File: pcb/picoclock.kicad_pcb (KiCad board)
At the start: 2 copper layers, 175.8 x 64 mm, 87 parts, among them J1 UART, J10 USB, J11 Alt Power, J12 PWM, J13 AUDIO, J15 Conn_01x24, J2 AUDIO, J3 xx, J4 xx, J5 Micro_SD_Card_Det1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

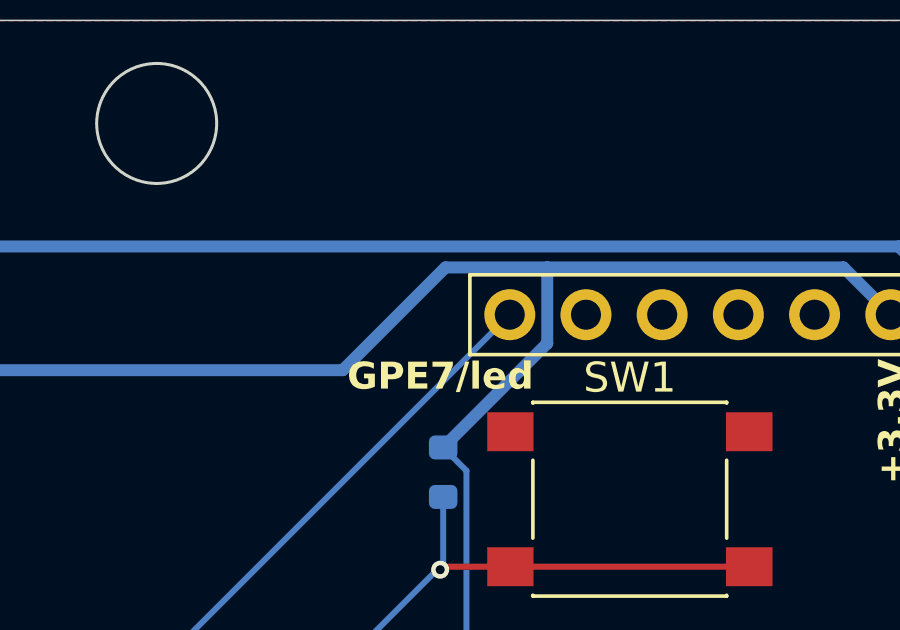
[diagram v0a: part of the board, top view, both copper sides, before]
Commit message: [pcb] add pullup resistor for MCP23009
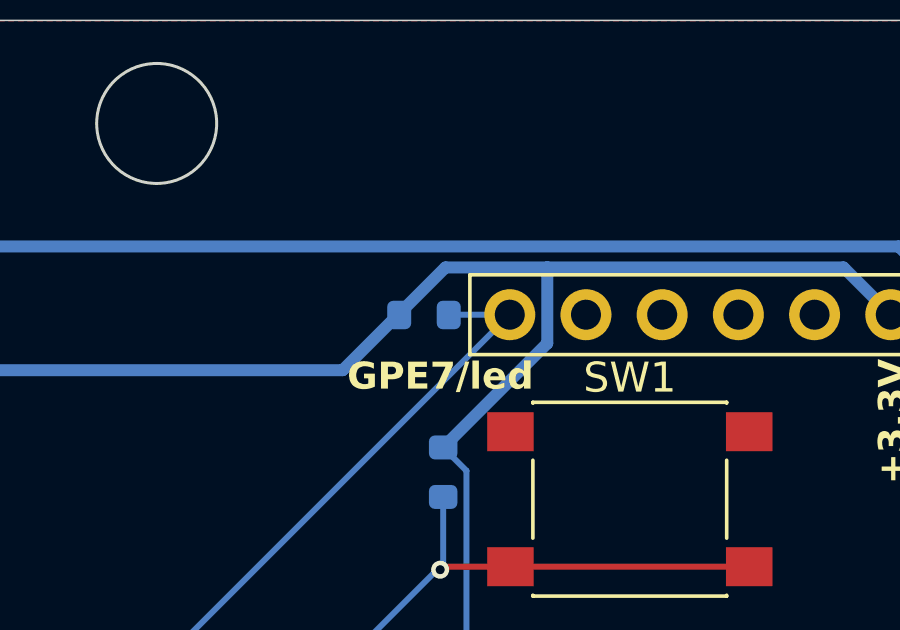
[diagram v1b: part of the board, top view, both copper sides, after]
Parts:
- added R17: 10K, Resistor_SMD:R_0603_1608Metric, B.Cu at (188.5, 76.7)
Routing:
- net GPE7/led: track 54.3 -> 56.4 mm
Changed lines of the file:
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@@
 		)
 	)
+	(footprint "Resistor_SMD:R_0603_1608Metric"
+		(layer "B.Cu")
+		(at 188.46 76.71)
+		(descr "Resistor SMD 0603 (1608 Metric), square (rectangular) end terminal, IPC_7351 nominal, (Body size source: IPC-SM-782 page 72, https://www.pcb-3d.com/wordpress/wp-content/uploads/ipc-sm-782a_amendment_1_and_2.pdf), generated with kicad-footprint-generator")
+		(tags "resistor")
+		(property "Reference" "R17"
+			(at -2.83 -0.04 360)
+			(layer "B.SilkS")
+			(effects
+				(font
+					(size 1 1)
+					(thickness 0.15)
+				)
+				(justify mirror)
+			)
+		)
+		(property "Value" "10K"
+			(at -5.86 -0.01 0)
+			(layer "B.SilkS")
+			(effects
+				(font
+					(size 1 1)
+					(thickness 0.15)
+				)
+				(justify mirror)
+			)
+		)
+		(property "Footprint" "Resistor_SMD:R_0603_1608Metric"
+			(at 0 0 180)
+			(unlocked yes)
+			(layer "B.Fab")
+			(hide yes)
+			(effects
+				(font
+					(size 1.27 1.27)
+					(thickness 0.15)
+				)
+				(justify mirror)
+			)
+		)
+		(property "Datasheet" ""
+			(at 0 0 180)
+			(unlocked yes)
+			(layer "B.Fab")
+			(hide yes)
+			(effects
+				(font
+					(size 1.27 1.27)
+					(thickness 0.15)
+				)
+				(justify mirror)
+			)
+		)
+		(property "Description" ""
+			(at 0 0 180)
+			(unlocked yes)
+			(layer "B.Fab")
+			(hide yes)
+			(effects
+				(font
+					(size 1.27 1.27)
+					(thickness 0.15)
+				)
+				(justify mirror)
+			)
+		)
+		(property "LCSC" "C25744"
+			(at 0 0 180)
+			(unlocked yes)
+			(layer "B.Fab")
+			(hide yes)
+			(effects
+				(font
+					(size 1 1)
+					(thickness 0.15)
+				)
+				(justify mirror)
+			)
+		)
+		(property ki_fp_filters "R_*")
+		(sheetname "Root")
+		(sheetfile "picoclock.kicad_sch")
+		(attr smd)
+		(fp_line
+			(start 0.237258 -0.5225)
+			(end -0.237258 -0.5225)
+			(stroke
+				(width 0.12)
+				(type solid)
+			)
+			(layer "B.SilkS")
+		)
+		(fp_line
+			(start 0.237258 0.5225)
+			(end -0.237258 0.5225)
+			(stroke
+				(width 0.12)
+				(type solid)
+			)
+			(layer "B.SilkS")
+		)
+		(fp_line
+			(start -1.48 -0.73)
+			(end 1.48 -0.73)
+			(stroke
+				(width 0.05)
+				(type solid)
+			)
+			(layer "B.CrtYd")
+		)
+		(fp_line
+			(start -1.48 0.73)
+			(end -1.48 -0.73)
+			(stroke
+				(width 0.05)
+				(type solid)
+			)
+			(layer "B.CrtYd")
+		)
+		(fp_line
+			(start 1.48 -0.73)
+			(end 1.48 0.73)
+			(stroke
+				(width 0.05)
+				(type solid)
+			)
+			(layer "B.CrtYd")
+		)
+		(fp_line
+			(start 1.48 0.73)
+			(end -1.48 0.73)
+			(stroke
+				(width 0.05)
+				(type solid)
+			)
+			(layer "B.CrtYd")
+		)
+		(fp_line
+			(start -0.8 -0.4125)
+			(end 0.8 -0.4125)
+			(stroke
+				(width 0.1)
+				(type solid)
+			)
+			(layer "B.Fab")
+		)
+		(fp_line
+			(start -0.8 0.4125)
+			(end -0.8 -0.4125)
+			(stroke
+				(width 0.1)
+				(type solid)
+			)
+			(layer "B.Fab")
+		)
+		(fp_line
+			(start 0.8 -0.4125)
+			(end 0.8 0.4125)
+			(stroke
+				(width 0.1)
+				(type solid)
+			)
+			(layer "B.Fab")
+		)
+		(fp_line
+			(start 0.8 0.4125)
+			(end -0.8 0.4125)
+			(stroke
+				(width 0.1)
+				(type solid)
+			)
+			(layer "B.Fab")
+		)
+		(fp_text user "${REFERENCE}"
+			(at 0 0 360)
+			(layer "B.Fab")
+			(effects
+				(font
+					(size 0.4 0.4)
+					(thickness 0.06)
+				)
+				(justify mirror)
+			)
+		)
+		(pad "1" smd roundrect
+			(at -0.825 0)
+			(size 0.8 0.95)
+			(layers "B.Cu" "B.Paste" "B.Mask")
+			(roundrect_rratio 0.25)
+			(net 2 "+3.3V")
+			(pintype "passive")
+		)
+		(pad "2" smd roundrect
+			(at 0.825 0)
+			(size 0.8 0.95)
+			(layers "B.Cu" "B.Paste" "B.Mask")
+			(roundrect_rratio 0.25)
+			(net 55 "GPE7{slash}led")
+			(pintype "passive")
+		)
+		(model "${KICAD8_3DMODEL_DIR}/Resistor_SMD.3dshapes/R_0603_1608Metric.wrl"
+			(offset
+				(xyz 0 0 0)
+			)
+			(scale
+				(xyz 1 1 1)
+			)
+			(rotate
+				(xyz 0 0 0)
+			)
+		)
+	)
 	(footprint "Capacitor_SMD:C_0603_1608Metric"
 		(layer "B.Cu")
@@
 		)
 	)
-	(gr_text "+3.3V"
-		(at 189.3955 72.375 90)
-		(layer "B.SilkS")
-		(effects
-			(font
-				(size 0.9 0.9)
-				(thickness 0.15)
-				(bold yes)
-			)
-			(justify left bottom mirror)
-		)
-	)
 	(gr_text "CLK"
 		(at 170.425 83.025 0)
@@
 		(width 0.2)
 		(layer "B.Cu")
+		(net 55)
+	)
+	(segment
+		(start 189.295 76.7)
+		(end 189.285 76.71)
+		(width 0.2)
+		(layer "B.Cu")
+		(net 55)
+	)
+	(segment
+		(start 191.32 76.7)
+		(end 189.295 76.7)
+		(width 0.2)
+		(layer "B.Cu")

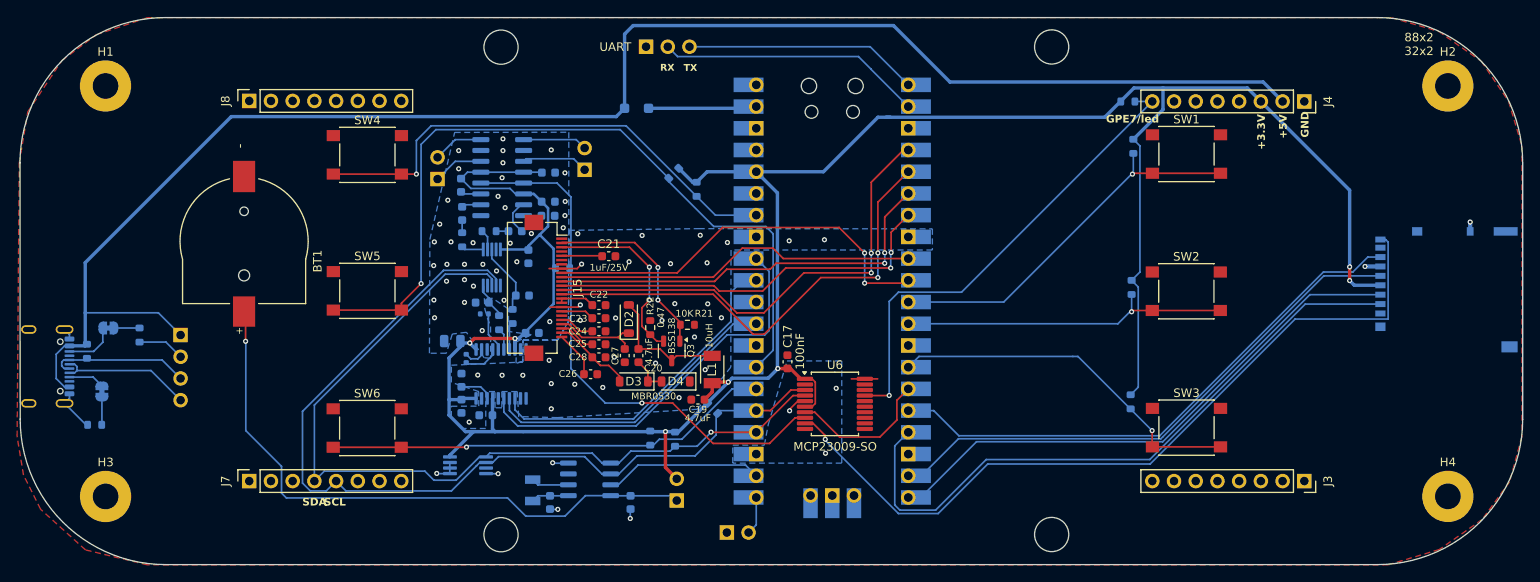
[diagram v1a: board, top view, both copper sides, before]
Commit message: [pcb] move battery holder, other small tweaks
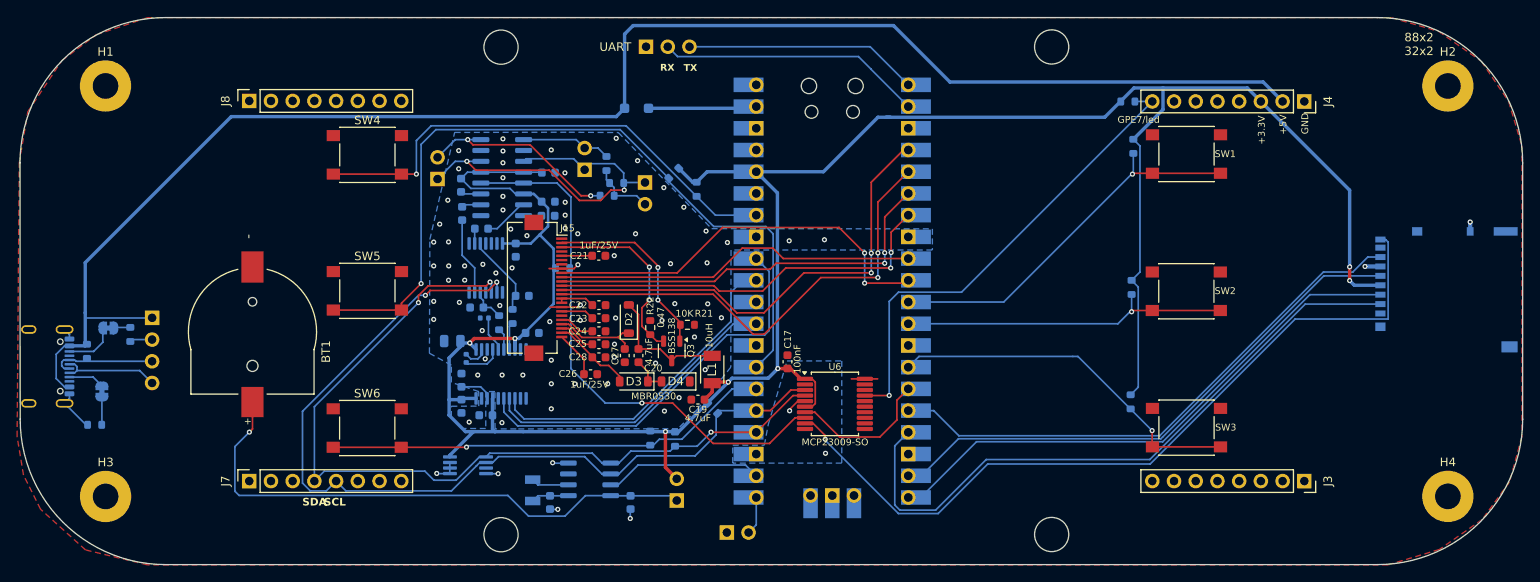
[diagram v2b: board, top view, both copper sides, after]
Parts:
- added J9: AUDIO, Connector_PinHeader_2.54mm:PinHeader_1x02_P2.54mm_Vertical, B.Cu at (132.0, 86.2)
- added R18: 10K, Resistor_SMD:R_0603_1608Metric, B.Cu at (128.7, 86.2)
- R14, R15: value 470 -> 10K
- U7: value MCP4652T -> MCP4652-104E; footprint Package_SO:MSOP-10_3x3mm_P0.5mm -> Package_SO:TSSOP-14_4.4x5mm_P0.65mm
- moved R14 17.7 mm to (127.6, 87.7), turned to 180 degrees
- moved R15 15.8 mm to (127.5, 84.0), turned to 90 degrees
- moved BT1 10.6 mm to (86.1, 103.6)
- moved C18 3.95 mm to (112.9, 91.6)
- moved J10 3.89 mm to (74.3, 102.0)
- moved C15 1.66 mm to (116.9, 94.1)
- moved C21 1.17 mm to (126.6, 94.8)
- moved R5 1.08 mm to (71.8, 104.0)
- moved C10 0.86 mm to (112.3, 100.8)
- moved U7 0.71 mm to (113.4, 96.2)
- moved C8 0.48 mm to (113.2, 102.0)
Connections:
- C18 pad 1: Net-(C18-Pad1) -> Net-(U7-P0W)
- C29 pad 1: Net-(C29-Pad1) -> Net-(U7-P1W)
- J2 pad 1: AUDIO_OUT_R- -> AUDIO_OUT_L-
- R14 pad 1: Net-(U7-P1W) -> MONO_OUT_R+
- R14 pad 2: Net-(C29-Pad1) -> AUDIO_OUT_R+
- R15 pad 1: Net-(C18-Pad1) -> MONO_OUT_R+
- R15 pad 2: Net-(U7-P0W) -> AUDIO_OUT_L+
- U5 pad 14: AUDIO_OUT_R- -> AUDIO_OUT_L-
- U7 pad 10: +3.3V -> LINE_OUT_RIGHT
- U7 pad 7: Net-(U7-P0W) -> GND
- U7 pad 8: LINE_OUT_RIGHT -> GND
- U7 pad 9: GND -> Net-(U7-P0W)
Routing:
- net AUDIO_OUT_L-: track 7.79 -> 44.4 mm, vias 0 -> 2
- net AUDIO_OUT_R+: track 5.92 -> 24.1 mm, vias 0 -> 2
- net MONO_OUT_R+: track 0.00 -> 7.33 mm
- net Net-(U7-P1W): track 2.60 -> 9.07 mm
- net 3V BATT: track 71.7 -> 65.5 mm
- net AUDIO_OUT_R-: track 5.92 -> 0.00 mm
- net +5V: track 190.9 -> 186.5 mm
- net USB D-: track 16.0 -> 11.8 mm
- net USB D+: track 16.4 -> 12.2 mm
- net GND: track 38.6 -> 35.4 mm, vias 76 -> 82
- net AUDIO_OUT_L+: track 7.54 -> 10.5 mm
- net Net-(C29-Pad1): track 1.47 -> 0.00 mm
- net Net-(C18-Pad1): track 1.45 -> 0.00 mm
- net LINE_OUT_RIGHT: track 8.33 -> 9.57 mm
- net Net-(J15-Pin_5): track 4.75 -> 3.56 mm
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
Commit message: [pcb] mono audio, combined sdcard footprint
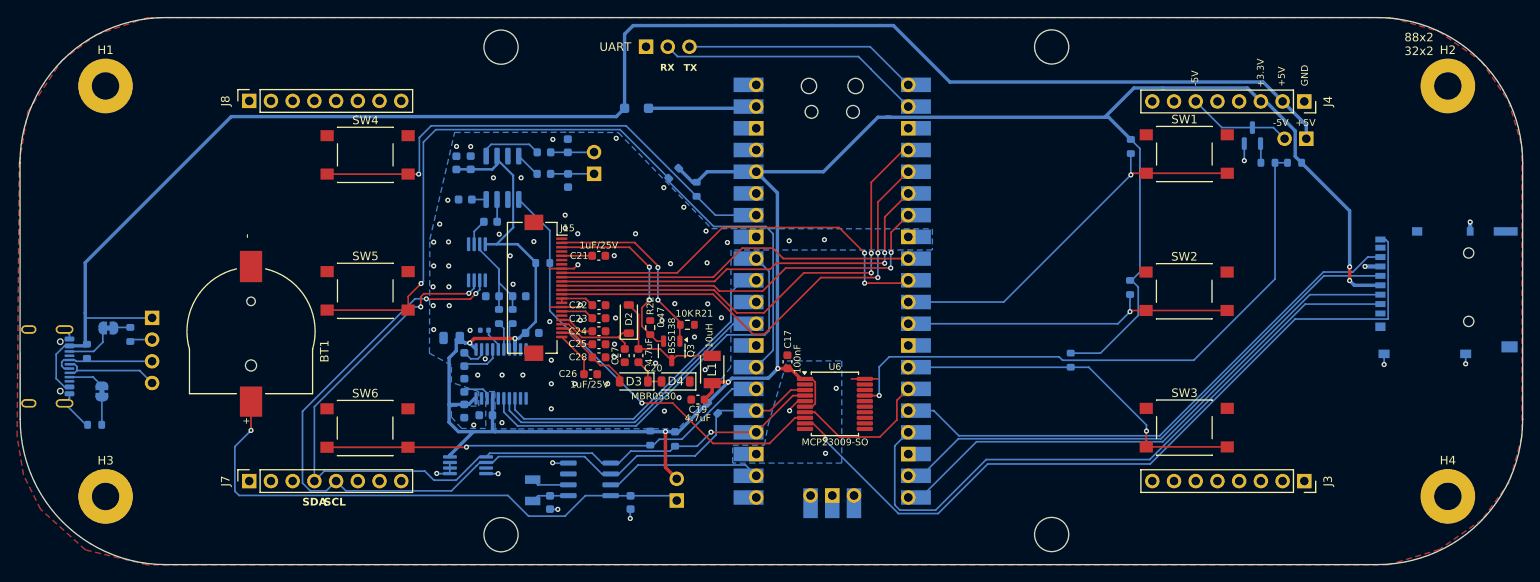
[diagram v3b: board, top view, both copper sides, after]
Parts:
- removed C13: 1uF, Capacitor_SMD:C_0603_1608Metric
- removed C16: 470uF, Capacitor_SMD:C_0603_1608Metric
- removed J13, J2: AUDIO, Connector_PinHeader_2.54mm:PinHeader_1x02_P2.54mm_Vertical
- removed R14, R15, R18: 10K, Resistor_SMD:R_0603_1608Metric
- added C30: 220pF, Capacitor_SMD:C_0603_1608Metric, B.Cu at (123.0, 81.9)
- added FB1: FerriteBead, Inductor_SMD:L_0603_1608Metric, B.Cu at (120.2, 82.7)
- added FB2: FerriteBead, Inductor_SMD:L_0603_1608Metric, B.Cu at (120.2, 85.2)
- added Q1: BSS138, Package_TO_SOT_SMD:SOT-23, B.Cu at (203.0, 80.7)
- added R19: 1K, Resistor_SMD:R_0603_1608Metric, B.Cu at (204.8, 83.9)
- C15: value 1uF -> 10uF
- C29: value 4.7uF -> 220pF
- C7: footprint Capacitor_SMD:C_0402_1005Metric -> Capacitor_SMD:C_0603_1608Metric
- H1, H2, H3, H4: footprint MountingHole:MountingHole_3mm_Pad -> MountingHole:MountingHole_3.2mm_M3_Pad
- J12: value PWM -> LED_5V
- J5: footprint Connector_Card:microSD_HC_Hirose_DM3AT-SF-PEJM5 -> clock:microSD_HC_Hirose_DM3AT-SF-PEJM5_combined_MSD-4-A
- SW1, SW2, SW3, SW4, SW5, SW6: footprint Button_Switch_SMD:SW_SPST_PTS645 -> clock:SW_SPST_TL3301TG
- U5: value PAM8403D -> PAM8302A; footprint Package_SO:SOP-16_3.9x9.9mm_P1.27mm -> Package_SO:SOP-8_3.76x4.96mm_P1.27mm
- U7: value MCP4652-104E -> MCP45X1-104E; footprint Package_SO:TSSOP-14_4.4x5mm_P0.65mm -> Package_SO:MSOP-8_3x3mm_P0.65mm
- moved J12 81.9 mm to (209.3, 81.1), turned to 90 degrees
- moved R17 20.8 mm to (208.0, 83.9), turned to 180 degrees
- moved C29 13.0 mm to (123.0, 85.9), turned to -90 degrees
- moved C15 12.3 mm to (109.9, 83.9), turned to 90 degrees
- moved C12 9.88 mm to (111.0, 88.2), turned to 180 degrees
- moved R12 8.54 mm to (181.8, 107.0)
- moved J9 6.05 mm to (126.0, 85.2), turned to 0 degrees
- moved C14 2.87 mm to (111.6, 83.9), turned to 90 degrees
- moved R16 2.40 mm to (120.0, 95.6)
- moved C10 2.26 mm to (114.1, 99.5)
- moved C8 1.43 mm to (113.2, 103.5)
- moved C18 1.33 mm to (113.9, 90.8)
- moved U7 1.23 mm to (112.3, 95.5)
- moved R2 0.72 mm to (114.9, 101.9)
- moved C9 0.69 mm to (110.9, 109.9)
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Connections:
- C10 pad 2: LINE_OUT_LEFT -> MONO_OUT+
- C11 pad 2: LINE_OUT_RIGHT -> MONO_OUT+
- C12 pad 1: Net-(U5-VREF) -> Net-(U5-IN-)
- C18 pad 2: LOL_ADJ -> Net-(U5-IN+)
- C29 pad 1: Net-(U7-P1W) -> MONO_OUT_R-
- C29 pad 2: LOR_ADJ -> GND
- D1 pad 2: +5V -> LED_5V+
- J10 pad 1: +5V -> LED_5V+
- J12 pad 1: GND -> LED_5V+
- J12 pad 2: GPIO16 / PWM -> LED_5V-
- J4 pad 2: +5V -> LED_5V+
- J4 pad 6: unconnected-(J4-Pin_6-Pad6) -> LED_5V-
- J4 pad 8: GPE7/led -> unconnected-(J4-Pin_8-Pad8)
- J6 pad A4: +5V -> LED_5V+
- J6 pad A9: +5V -> LED_5V+
- J6 pad B4: +5V -> LED_5V+
- J6 pad B9: +5V -> LED_5V+
- J9 pad 1: AUDIO_OUT_L- -> MONO_OUT_R-
- R2 pad 2: LINE_OUT_LEFT -> MONO_OUT+
- R4 pad 2: LINE_OUT_RIGHT -> MONO_OUT+
- R7 pad 2: +5V -> LED_5V+
- U2 pad 21: GPIO16 / PWM -> unconnected-(U2-GPIO16-Pad21)
- U5 pad 1: AUDIO_OUT_L+ -> MUTE
- U5 pad 2: GND -> unconnected-(U5-NC-Pad2)
- U5 pad 3: AUDIO_OUT_L- -> Net-(U5-IN+)
- U5 pad 4: +3.3V -> Net-(U5-IN-)
- U5 pad 5: MUTE -> Net-(U5-OUT+)
- U5 pad 7: LOL_ADJ -> GND
- U5 pad 8: Net-(U5-VREF) -> Net-(U5-OUT-)
- U7 pad 5: LINE_OUT_LEFT -> GND
- U7 pad 6: Net-(U7-P1W) -> Net-(U7-P0W)
- U7 pad 7: GND -> MONO_OUT+
- U7 pad 8: GND -> +3.3V
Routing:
- net LED_5V+: track 0.00 -> 192.0 mm
- net +5V: track 186.5 -> 0.00 mm
- net AUDIO_OUT_L-: track 44.4 -> 0.00 mm, vias 2 -> 0
- net AUDIO_OUT_R+: track 24.1 -> 0.00 mm, vias 2 -> 0
- net GPE7/led: track 56.4 -> 71.0 mm
- net MONO_OUT+: track 0.00 -> 13.8 mm
- net LED_5V-: track 0.00 -> 11.6 mm
- net MUTE: track 63.5 -> 52.0 mm
- net +3.3V: track 303.5 -> 292.2 mm
- net AUDIO_OUT_L+: track 10.5 -> 0.00 mm
- net LINE_OUT_RIGHT: track 9.57 -> 0.00 mm
- net Net-(U7-P1W): track 9.07 -> 0.00 mm
- net Net-(U5-OUT+): track 0.00 -> 7.38 mm
- net LOL_ADJ: track 5.31 -> 0.00 mm
- net MONO_OUT_R-: track 0.00 -> 5.08 mm
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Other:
- board text added: "-5V"
- board text added: "AUDIO"
- board text removed: "AUDIO_L"
- board text removed: "AUDIO_R"
- board text removed: "GPE7/led"
